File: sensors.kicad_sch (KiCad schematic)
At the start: 10 parts, among them J12 GND, J13 Sensor, J14 3.3v, J15 SDA, J16 SCL, U33 BMI270

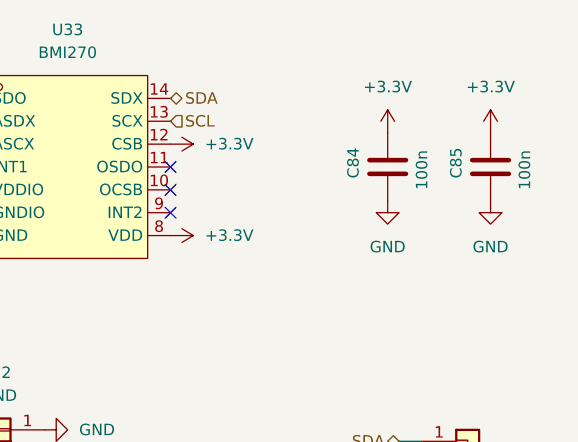
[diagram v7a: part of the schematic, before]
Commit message: Add extra capacitor next to LoRa module, fix review comments
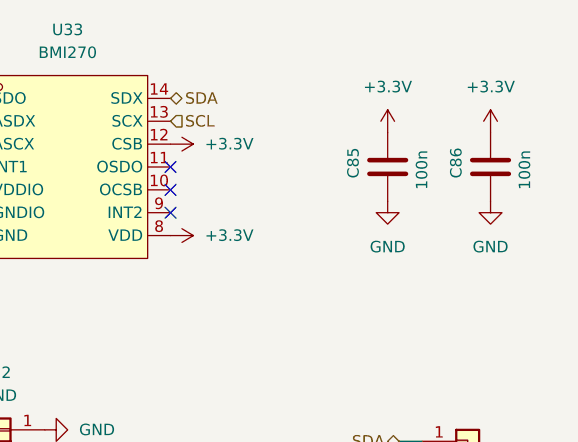
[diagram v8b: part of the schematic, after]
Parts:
- renumbered C84 to C85, C85 to C86
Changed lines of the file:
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@@
 	(title_block
 		(title "Tanmatsu")
-		(date "2025-04-04")
+		(date "2025-04-06")
 		(rev "1.0")
 		(company "Nicolai Electronics")
@@
 		(dnp no)
 		(fields_autoplaced yes)
-		(property "Reference" "#PWR0299"
+		(property "Reference" "#PWR0300"
 			(at 45.72 73.66 0)
 			(effects
@@
 			(project "why2025"
 				(path "/6a31734e-65de-48f3-8156-2b24b665b183/14d9c0ee-00ab-4a1b-b059-e8045c71d6ae"
-					(reference "#PWR0299")
+					(reference "#PWR0300")
 					(unit 1)
 				)
@@
 		(on_board yes)
 		(dnp no)
-		(property "Reference" "#PWR0293"
+		(property "Reference" "#PWR0294"
 			(at 87.63 44.45 0)
 			(effects
@@
 			(project "why2025"
 				(path "/6a31734e-65de-48f3-8156-2b24b665b183/14d9c0ee-00ab-4a1b-b059-e8045c71d6ae"
-					(reference "#PWR0293")
+					(reference "#PWR0294")
 					(unit 1)
 				)
@@
 		(dnp no)
 		(fields_autoplaced yes)
-		(property "Reference" "#PWR0295"
+		(property "Reference" "#PWR0296"
 			(at 59.69 41.91 0)
 			(effects
@@
 			(project "why2025"
 				(path "/6a31734e-65de-48f3-8156-2b24b665b183/14d9c0ee-00ab-4a1b-b059-e8045c71d6ae"
-					(reference "#PWR0295")
+					(reference "#PWR0296")
 					(unit 1)
 				)
@@
 		(dnp no)
 		(fields_autoplaced yes)
-		(property "Reference" "#PWR0291"
+		(property "Reference" "#PWR0292"
 			(at 59.69 31.75 0)
 			(effects
@@
 			(project "why2025"
 				(path "/6a31734e-65de-48f3-8156-2b24b665b183/14d9c0ee-00ab-4a1b-b059-e8045c71d6ae"
-					(reference "#PWR0291")
+					(reference "#PWR0292")
 					(unit 1)
 				)
@@
 		(dnp no)
 		(fields_autoplaced yes)
-		(property "Reference" "#PWR0297"
+		(property "Reference" "#PWR0298"
 			(at 55.88 63.5 0)
 			(effects
@@
 			(project "why2025"
 				(path "/6a31734e-65de-48f3-8156-2b24b665b183/14d9c0ee-00ab-4a1b-b059-e8045c71d6ae"
-					(reference "#PWR0297")
+					(reference "#PWR0298")
 					(unit 1)
 				)
@@
 		(on_board yes)
 		(dnp no)
-		(property "Reference" "C84"
+		(property "Reference" "C85"
 			(at 83.82 35.56 90)
 			(effects
@@
 			(project "why2025"
 				(path "/6a31734e-65de-48f3-8156-2b24b665b183/14d9c0ee-00ab-4a1b-b059-e8045c71d6ae"
-					(reference "C84")
+					(reference "C85")
 					(unit 1)
 				)
@@
 		(dnp no)
 		(fields_autoplaced yes)
-		(property "Reference" "#PWR0289"
+		(property "Reference" "#PWR0290"
 			(at 87.63 34.29 0)
 			(effects
@@
 			(project "why2025"
 				(path "/6a31734e-65de-48f3-8156-2b24b665b183/14d9c0ee-00ab-4a1b-b059-e8045c71d6ae"
-					(reference "#PWR0289")
+					(reference "#PWR0290")
 					(unit 1)
 				)
@@
 		(dnp no)
 		(fields_autoplaced yes)
-		(property "Reference" "#PWR0290"
+		(property "Reference" "#PWR0291"
 			(at 99.06 34.29 0)
 			(effects
@@
 			(project "why2025"
 				(path "/6a31734e-65de-48f3-8156-2b24b665b183/14d9c0ee-00ab-4a1b-b059-e8045c71d6ae"
-					(reference "#PWR0290")
+					(reference "#PWR0291")
 					(unit 1)
 				)
@@
 		(dnp no)
 		(fields_autoplaced yes)
-		(property "Reference" "#PWR0298"
+		(property "Reference" "#PWR0299"
 			(at 92.71 69.85 0)
 			(effects
@@
 			(project "tanmatsu"
 				(path "/6a31734e-65de-48f3-8156-2b24b665b183/14d9c0ee-00ab-4a1b-b059-e8045c71d6ae"
-					(reference "#PWR0298")
+					(reference "#PWR0299")
 					(unit 1)
 				)
@@
 		(on_board yes)
 		(dnp no)
-		(property "Reference" "#PWR0296"
+		(property "Reference" "#PWR0297"
 			(at 38.1 50.8 0)
 			(effects
@@
 			(project "why2025"
 				(path "/6a31734e-65de-48f3-8156-2b24b665b183/14d9c0ee-00ab-4a1b-b059-e8045c71d6ae"
-					(reference "#PWR0296")
+					(reference "#PWR0297")
 					(unit 1)
 				)
@@
 		(dnp no)
 		(fields_autoplaced yes)
-		(property "Reference" "#PWR0292"
+		(property "Reference" "#PWR0293"
 			(at 31.75 36.83 0)
 			(effects
@@
 			(project "why2025"
 				(path "/6a31734e-65de-48f3-8156-2b24b665b183/14d9c0ee-00ab-4a1b-b059-e8045c71d6ae"
-					(reference "#PWR0292")
+					(reference "#PWR0293")
 					(unit 1)
 				)
@@
 		(dnp no)
 		(fields_autoplaced yes)
-		(property "Reference" "#PWR0300"
+		(property "Reference" "#PWR0301"
 			(at 88.9 81.28 0)
 			(effects
@@
 			(project "tanmatsu"
 				(path "/6a31734e-65de-48f3-8156-2b24b665b183/14d9c0ee-00ab-4a1b-b059-e8045c71d6ae"
-					(reference "#PWR0300")
+					(reference "#PWR0301")
 					(unit 1)
 				)
@@
 		(on_board yes)
 		(dnp no)
-		(property "Reference" "#PWR0294"
+		(property "Reference" "#PWR0295"
 			(at 99.06 44.45 0)
 			(effects
@@
 			(project "why2025"
 				(path "/6a31734e-65de-48f3-8156-2b24b665b183/14d9c0ee-00ab-4a1b-b059-e8045c71d6ae"
-					(reference "#PWR0294")
+					(reference "#PWR0295")
 					(unit 1)
 				)
@@
 		(dnp no)
 		(fields_autoplaced yes)
-		(property "Reference" "#PWR0288"
+		(property "Reference" "#PWR0289"
 			(at 34.29 27.94 0)
 			(effects
@@
 			(project "why2025"
 				(path "/6a31734e-65de-48f3-8156-2b24b665b183/14d9c0ee-00ab-4a1b-b059-e8045c71d6ae"
-					(reference "#PWR0288")
+					(reference "#PWR0289")
 					(unit 1)
 				)
@@
 		(on_board yes)
 		(dnp no)
-		(property "Reference" "C85"
+		(property "Reference" "C86"
 			(at 95.25 35.56 90)
 			(effects
@@
 			(project "why2025"
 				(path "/6a31734e-65de-48f3-8156-2b24b665b183/14d9c0ee-00ab-4a1b-b059-e8045c71d6ae"
-					(reference "C85")
-					(unit 1)
-				)
+					(reference "C86")
+					(unit 1)
+				)
